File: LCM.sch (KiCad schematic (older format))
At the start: 12 parts, among them J7 3-84952-0, J8 F52R-1A7H1-11020

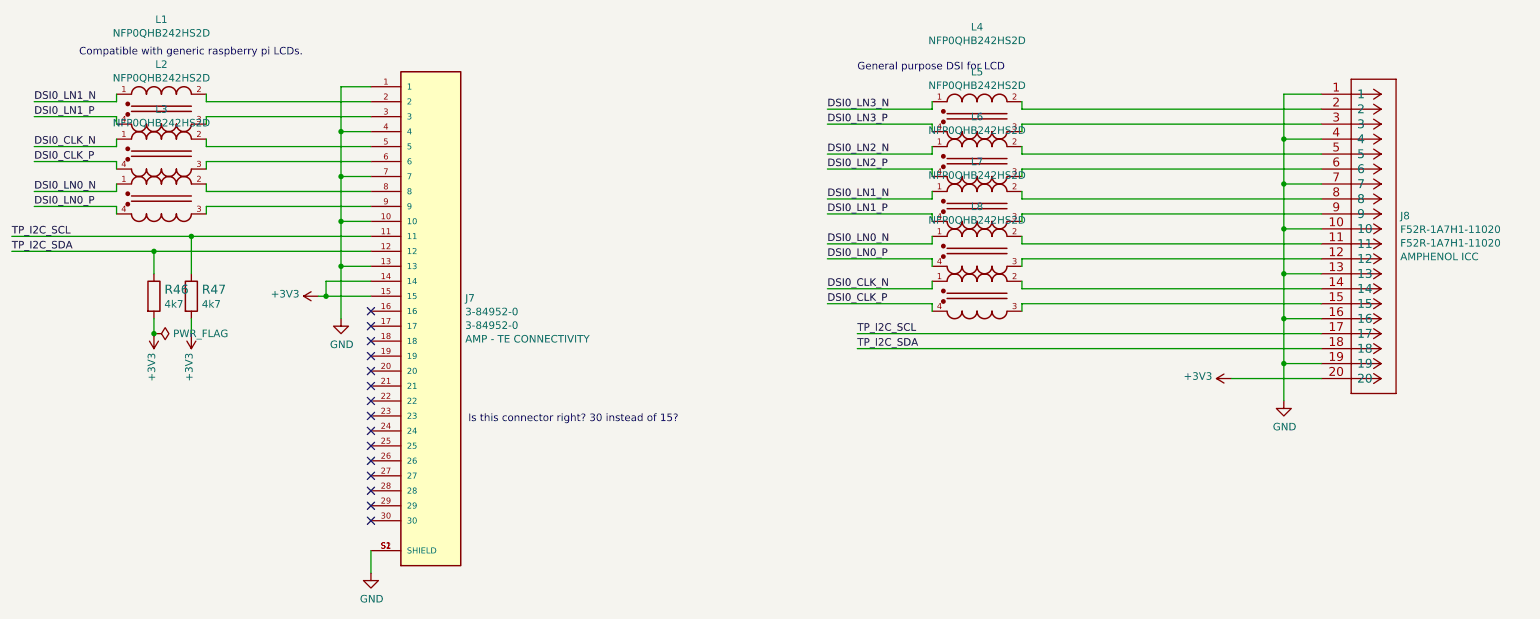
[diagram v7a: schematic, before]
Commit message: cleaned up components fields
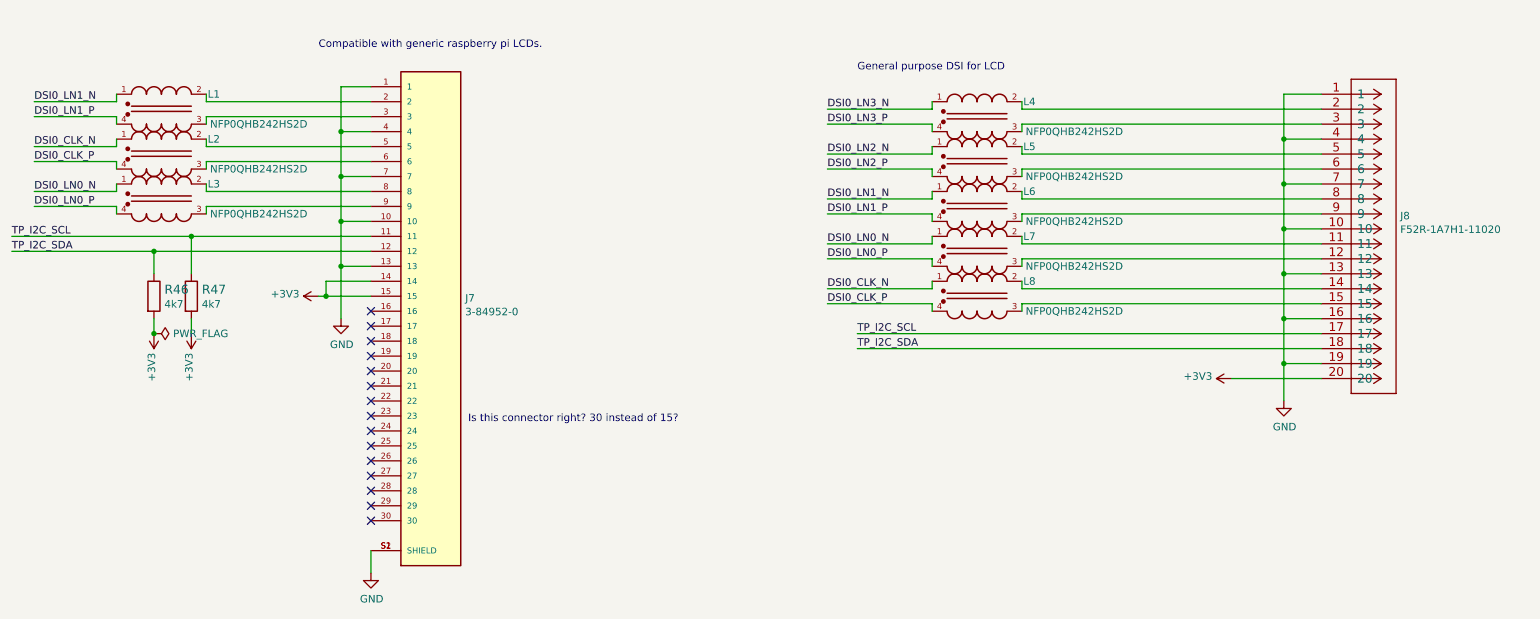
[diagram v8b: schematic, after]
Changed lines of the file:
@@
 F 2 "antmicro-footprints:TE_3-84952-0" H 4150 2250 50  0001 L BNN
 F 3 "https://www.te.com/commerce/DocumentDelivery/DDEController?Action=showdoc&DocId=Data+Sheet%7F1-1773959-6-flexible-printed-circuit-con%7F0919%7Fpdf%7FEnglish%7FENG_DS_1-1773959-6-flexible-printed-circuit-con_0919.pdf%7F3-84952-0" H 4150 2250 50  0001 L BNN
-F 4 "3-84952-0" H 3580 2155 50  0000 L CNN "MPN"
-F 5 "AMP - TE CONNECTIVITY" H 3580 2064 50  0000 L CNN "Manufacturer"
+F 4 "3-84952-0" H 3580 2155 50  0001 L CNN "MPN"
+F 5 "AMP - TE CONNECTIVITY" H 3580 2064 50  0001 L CNN "Manufacturer"
 	1    3350 2350
 	1    0    0    -1
@@
 Wire Wire Line
 	2950 4200 2950 4050
-Text Notes 1000 750  0    50   ~ 0
+Text Notes 2600 700  0    50   ~ 0
 Compatible with generic raspberry pi LCDs.
 Text Notes 3600 3200 0    50   ~ 0
@@
 F 2 "antmicro-footprints:F52R-1A7H1-11020" H 9500 900 50  0001 C CNN
 F 3 "https://www.snapeda.com/parts/F52R-1A7H1-11020/Amphenol%20ICC%20(FCI)/datasheet/" H 9500 900 50  0001 C CNN
-F 4 "F52R-1A7H1-11020" H 9828 -195 50  0000 L CNN "MPN"
-F 5 "AMPHENOL ICC" H 9828 -286 50  0000 L CNN "Manufacturer"
+F 4 "F52R-1A7H1-11020" H 9828 -195 50  0001 L CNN "MPN"
+F 5 "AMPHENOL ICC" H 9828 -286 50  0001 L CNN "Manufacturer"
 	1    9500 900
 	1    0    0    -1
@@
 AR Path="/61B9B38A" Ref="L?"  Part="1"
 AR Path="/61BD2CC1/61B9B38A" Ref="L1"  Part="1"
-F 0 "L1" H 1550 1699 50  0000 C CNN
-F 1 "NFP0QHB242HS2D" H 1550 1608 50  0000 C CNN
+F 0 "L1" H 1900 1200 50  0000 C CNN
+F 1 "NFP0QHB242HS2D" H 2200 1000 50  0000 C CNN
 F 2 "antmicro-footprints:FIL_NFP0QHB242HS2D" H 1550 1100 50  0001 C CNN
 F 3 "https://www.farnell.com/datasheets/2616945.pdf" H 1550 1100 50  0001 C CNN
@@
 AR Path="/61C048CC" Ref="L?"  Part="1"
 AR Path="/61BD2CC1/61C048CC" Ref="L2"  Part="1"
-F 0 "L2" H 1550 1999 50  0000 C CNN
-F 1 "NFP0QHB242HS2D" H 1550 1908 50  0000 C CNN
+F 0 "L2" H 1900 1500 50  0000 C CNN
+F 1 "NFP0QHB242HS2D" H 2200 1300 50  0000 C CNN
 F 2 "antmicro-footprints:FIL_NFP0QHB242HS2D" H 1550 1400 50  0001 C CNN
 F 3 "https://www.farnell.com/datasheets/2616945.pdf" H 1550 1400 50  0001 C CNN
@@
 AR Path="/61C3A309" Ref="L?"  Part="1"
 AR Path="/61BD2CC1/61C3A309" Ref="L3"  Part="1"
-F 0 "L3" H 1550 2299 50  0000 C CNN
-F 1 "NFP0QHB242HS2D" H 1550 2208 50  0000 C CNN
+F 0 "L3" H 1900 1800 50  0000 C CNN
+F 1 "NFP0QHB242HS2D" H 2200 1600 50  0000 C CNN
 F 2 "antmicro-footprints:FIL_NFP0QHB242HS2D" H 1550 1700 50  0001 C CNN
 F 3 "https://www.farnell.com/datasheets/2616945.pdf" H 1550 1700 50  0001 C CNN
@@
 AR Path="/61C65B0C" Ref="L?"  Part="1"
 AR Path="/61BD2CC1/61C65B0C" Ref="L4"  Part="1"
-F 0 "L4" H 7000 1749 50  0000 C CNN
-F 1 "NFP0QHB242HS2D" H 7000 1658 50  0000 C CNN
+F 0 "L4" H 7350 1250 50  0000 C CNN
+F 1 "NFP0QHB242HS2D" H 7650 1050 50  0000 C CNN
 F 2 "antmicro-footprints:FIL_NFP0QHB242HS2D" H 7000 1150 50  0001 C CNN
 F 3 "https://www.farnell.com/datasheets/2616945.pdf" H 7000 1150 50  0001 C CNN
@@
 AR Path="/61C82351" Ref="L?"  Part="1"
 AR Path="/61BD2CC1/61C82351" Ref="L5"  Part="1"
-F 0 "L5" H 7000 2049 50  0000 C CNN
-F 1 "NFP0QHB242HS2D" H 7000 1958 50  0000 C CNN
+F 0 "L5" H 7350 1550 50  0000 C CNN
+F 1 "NFP0QHB242HS2D" H 7650 1350 50  0000 C CNN
 F 2 "antmicro-footprints:FIL_NFP0QHB242HS2D" H 7000 1450 50  0001 C CNN
 F 3 "https://www.farnell.com/datasheets/2616945.pdf" H 7000 1450 50  0001 C CNN
@@
 AR Path="/61C82CCB" Ref="L?"  Part="1"
 AR Path="/61BD2CC1/61C82CCB" Ref="L6"  Part="1"
-F 0 "L6" H 7000 2349 50  0000 C CNN
-F 1 "NFP0QHB242HS2D" H 7000 2258 50  0000 C CNN
+F 0 "L6" H 7350 1850 50  0000 C CNN
+F 1 "NFP0QHB242HS2D" H 7650 1650 50  0000 C CNN
 F 2 "antmicro-footprints:FIL_NFP0QHB242HS2D" H 7000 1750 50  0001 C CNN
 F 3 "https://www.farnell.com/datasheets/2616945.pdf" H 7000 1750 50  0001 C CNN
@@
 AR Path="/61C832C1" Ref="L?"  Part="1"
 AR Path="/61BD2CC1/61C832C1" Ref="L7"  Part="1"
-F 0 "L7" H 7000 2649 50  0000 C CNN
-F 1 "NFP0QHB242HS2D" H 7000 2558 50  0000 C CNN
+F 0 "L7" H 7350 2150 50  0000 C CNN
+F 1 "NFP0QHB242HS2D" H 7650 1950 50  0000 C CNN
 F 2 "antmicro-footprints:FIL_NFP0QHB242HS2D" H 7000 2050 50  0001 C CNN
 F 3 "https://www.farnell.com/datasheets/2616945.pdf" H 7000 2050 50  0001 C CNN
@@
 AR Path="/61C83C74" Ref="L?"  Part="1"
 AR Path="/61BD2CC1/61C83C74" Ref="L8"  Part="1"
-F 0 "L8" H 7000 2949 50  0000 C CNN
-F 1 "NFP0QHB242HS2D" H 7000 2858 50  0000 C CNN
+F 0 "L8" H 7350 2450 50  0000 C CNN
+F 1 "NFP0QHB242HS2D" H 7650 2250 50  0000 C CNN
 F 2 "antmicro-footprints:FIL_NFP0QHB242HS2D" H 7000 2350 50  0001 C CNN
 F 3 "https://www.farnell.com/datasheets/2616945.pdf" H 7000 2350 50  0001 C CNN
